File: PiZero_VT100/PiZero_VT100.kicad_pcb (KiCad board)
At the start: 2 copper layers, 99.7 x 99.9 mm, 32 parts, among them J1 GPIO, J2 RS232, J3 Ext. Power max,. 9V DC/AC, J4 Mini-DIN-6, J5 to Testpins 22(DM) and TP23(D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, J6 USB_A, J7 Z80-MBC2 direct, J8 LCD Power, J9 On / Off, K1 G5V-2, Q1 BC547, U1 LM350_TO220

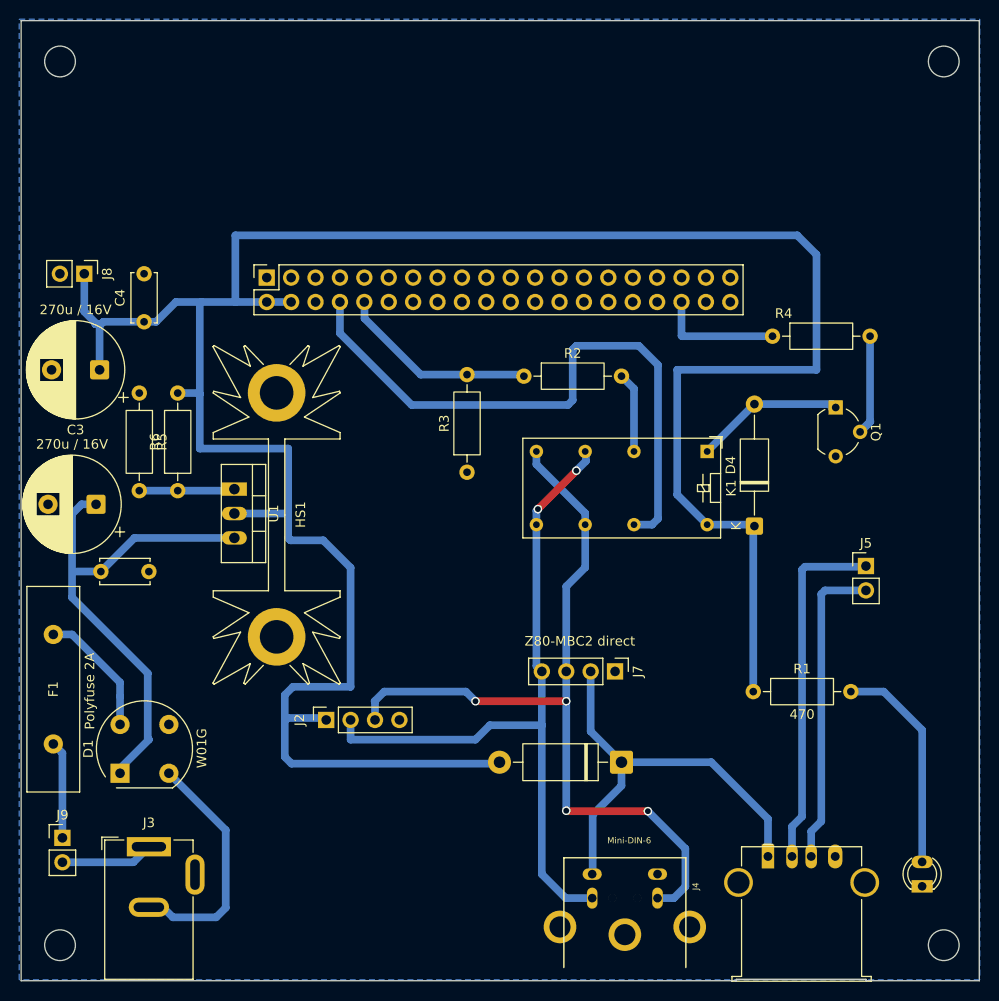
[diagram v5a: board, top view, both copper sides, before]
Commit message: Summer berücksichtig Layout für Fertigung bei PCBWays
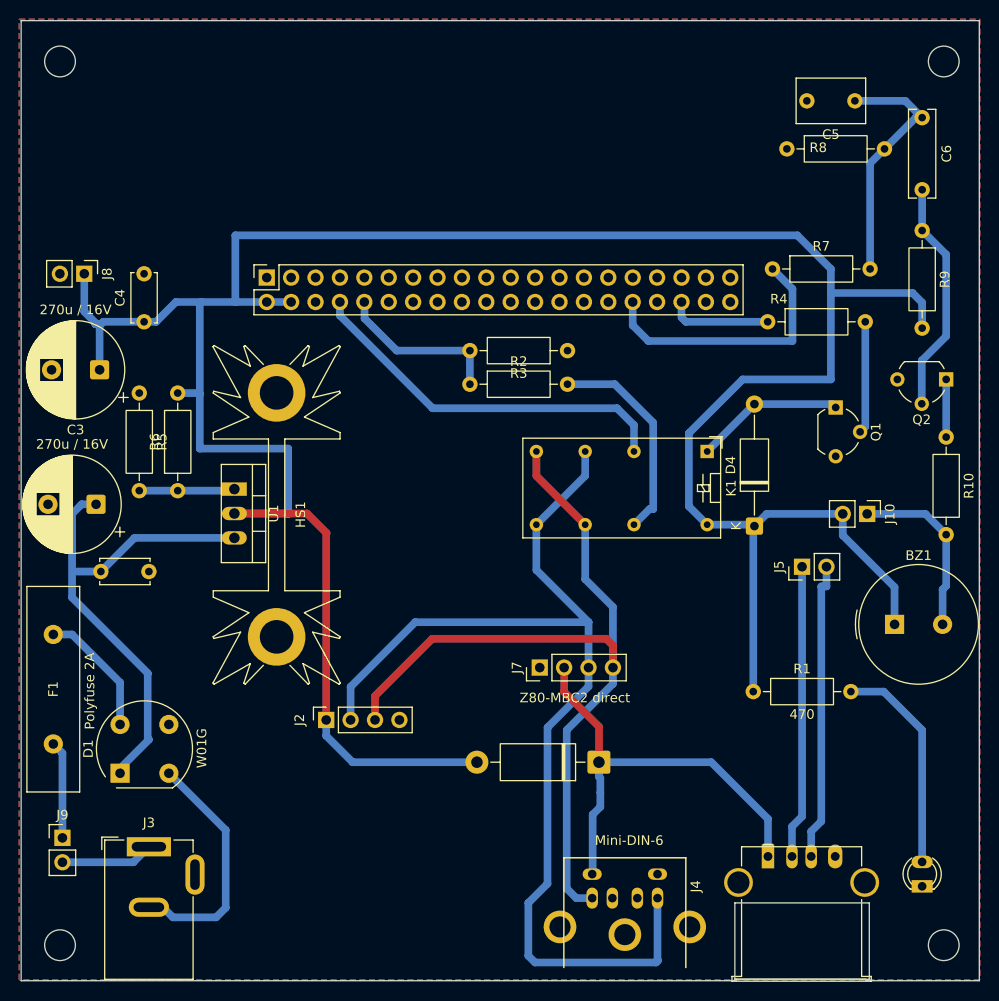
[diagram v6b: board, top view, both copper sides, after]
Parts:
- added BZ1: Buzzer, Buzzer_Beeper:Buzzer_TDK_PS1240P02BT_D12.2mm_H6.5mm, F.Cu at (190.1, 131.5)
- added C5: 33n, Capacitor_THT:C_Rect_L7.0mm_W4.5mm_P5.00mm, F.Cu at (186.0, 77.0)
- added C6: 10u, Capacitor_THT:C_Rect_L9.0mm_W2.6mm_P7.50mm_MKT, F.Cu at (193.0, 78.8)
- added J10: 8 Ohm Speaker, Connector_PinHeader_2.54mm:PinHeader_1x02_P2.54mm_Vertical, F.Cu at (187.3, 120.0)
- added Q2: BC550, Package_TO_SOT_THT:TO-92_Wide, F.Cu at (195.5, 106.0)
- added R10: 10, Resistor_THT:R_Axial_DIN0207_L6.3mm_D2.5mm_P10.16mm_Horizontal, F.Cu at (195.5, 112.0)
- added R7: 100, Resistor_THT:R_Axial_DIN0207_L6.3mm_D2.5mm_P10.16mm_Horizontal, F.Cu at (177.4, 94.5)
- added R8: 150, Resistor_THT:R_Axial_DIN0207_L6.3mm_D2.5mm_P10.16mm_Horizontal, F.Cu at (178.9, 82.0)
- added R9: 15k, Resistor_THT:R_Axial_DIN0207_L6.3mm_D2.5mm_P10.16mm_Horizontal, F.Cu at (193.0, 90.5)
- moved R3 16.4 mm to (156.1, 103.0), turned to 180 degrees
- moved J7 7.85 mm to (153.2, 136.0), turned to 90 degrees
- moved J5 6.65 mm to (180.5, 125.5), turned to 90 degrees
- moved R2 5.68 mm to (145.9, 106.5)
- moved D3 2.35 mm to (159.3, 145.8)
- moved R4 1.58 mm to (176.9, 100.0)
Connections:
- J1 pad 32: /GPIO12/PWM0 -> Sound
- J4 pad 3: Net-(J2-Pin_3) -> Net-(J2-Pin_2)
- J4 pad 4: Net-(J2-Pin_2) -> Net-(J2-Pin_3)
- J7 pad 3: Net-(J2-Pin_3) -> Net-(J2-Pin_2)
- J7 pad 4: Net-(J2-Pin_2) -> Net-(J2-Pin_3)
- K1 pad 13: /GPIO14/TXD0 -> Net-(K1-Pad13)
- K1 pad 4: Net-(K1-Pad4) -> /GPIO14/TXD0
- R2 pad 2: Net-(K1-Pad4) -> Net-(K1-Pad13)
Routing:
- net Net-(J2-Pin_2): track 75.2 -> 110.9 mm, vias 2 -> 0
- net Sound: track 0.00 -> 28.1 mm
- net Net-(C5-Pad1): track 0.00 -> 26.1 mm
- net /GPIO14/TXD0: track 64.7 -> 39.5 mm
- net Net-(Q2-B): track 0.00 -> 24.4 mm
- net Net-(K1-Pad13): track 0.00 -> 22.2 mm
- net Net-(BZ1--): track 0.00 -> 18.6 mm
- net +5V: track 269.6 -> 287.2 mm
- net Net-(K1-Pad4): track 8.38 -> 0.00 mm
- net Net-(J5-Pin_1): track 37.1 -> 30.6 mm
- net Net-(Q2-C): track 0.00 -> 6.00 mm
- net /GPIO15/RXD0: track 20.9 -> 17.6 mm
- net /GPIO16: track 13.0 -> 10.8 mm
- net Net-(D3-K): track 45.3 -> 47.4 mm
- net Net-(J2-Pin_3): track 84.4 -> 86.2 mm, vias 4 -> 0
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- added copper zone on F.Cu, net GND
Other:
- outline, holes or cut-outs redrawn
